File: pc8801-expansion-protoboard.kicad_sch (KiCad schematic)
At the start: 35 parts, among them J1 Solder Side, J2 Parts Side, J3 5V, J4 12V, J5 -12V, J6 GND_1, J7 GND_2, U1 ExpansionEdge, U10 74LS165, U11 ESP32-DEVKITC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

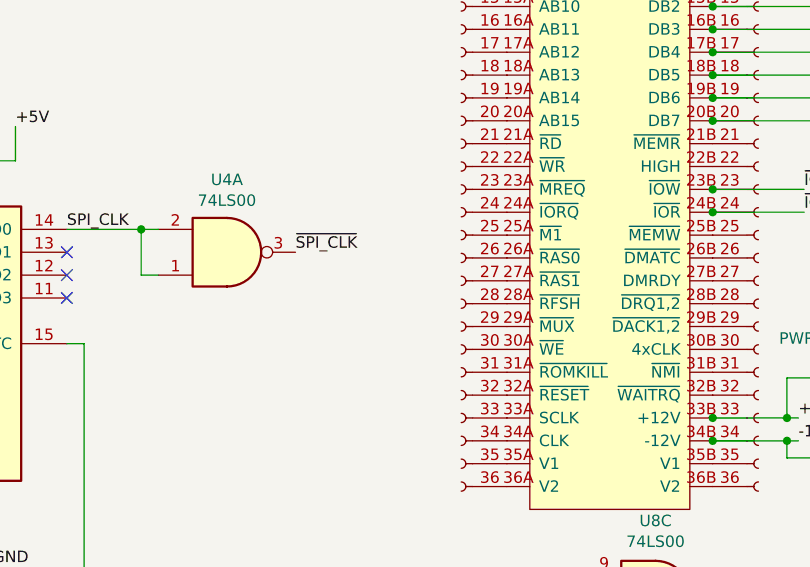
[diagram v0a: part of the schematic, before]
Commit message: Fix swapped-side near disaster
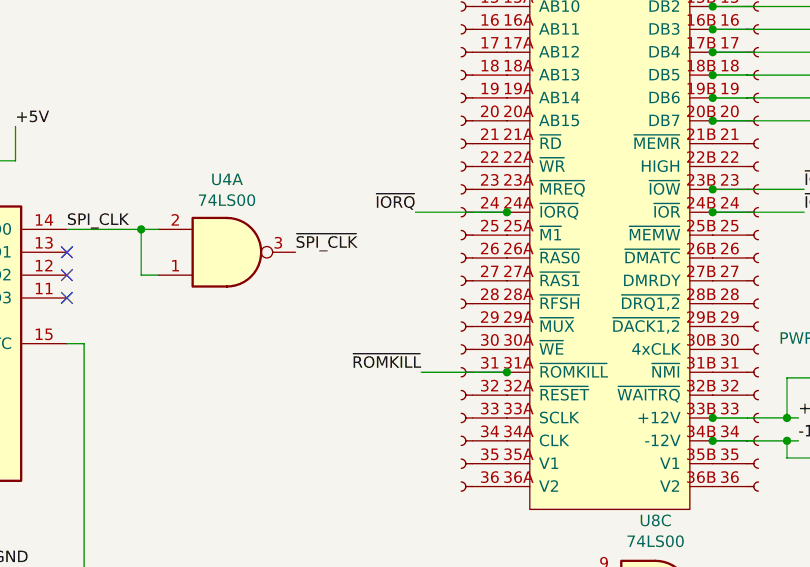
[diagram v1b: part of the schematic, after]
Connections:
- net ~{IORQ}: now reaches J1.24 (Pin_24), U1.24A (~{IORQ})
- net ~{ROMKILL}: now reaches J1.31 (Pin_31), U1.31A (~{ROMKILL})
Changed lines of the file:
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@@
   (junction (at 158.75 131.445) (diameter 0) (color 0 0 0 0)
   )
+  (junction (at 135.89 106.045) (diameter 0) (color 0 0 0 0)
+  )
   (junction (at 135.89 52.705) (diameter 0) (color 0 0 0 0)
   )
@@
   )
   (junction (at 135.89 60.325) (diameter 0) (color 0 0 0 0)
+  )
+  (junction (at 135.89 123.825) (diameter 0) (color 0 0 0 0)
   )
   (junction (at 231.14 133.35) (diameter 0) (color 0 0 0 0)
@@
     (stroke (width 0) (type default) (color 0 0 0 0))
   )
+  (wire (pts (xy 126.365 123.825) (xy 135.89 123.825))
+    (stroke (width 0) (type default) (color 0 0 0 0))
+  )
   (wire (pts (xy 81.28 96.52) (xy 81.28 100.33))
     (stroke (width 0) (type default) (color 0 0 0 0))
@@
   )
   (wire (pts (xy 55.88 163.195) (xy 55.88 160.02))
+    (stroke (width 0) (type default) (color 0 0 0 0))
+  )
+  (wire (pts (xy 125.73 106.045) (xy 135.89 106.045))
     (stroke (width 0) (type default) (color 0 0 0 0))
   )
@@
     (effects (font (size 1.27 1.27)) (justify right bottom))
   )
+  (label "~{IORQ}" (at 125.73 106.045 180)
+    (effects (font (size 1.27 1.27)) (justify right bottom))
+  )
   (label "D2" (at 179.705 83.185 0)
     (effects (font (size 1.27 1.27)) (justify left bottom))
@@
     (effects (font (size 1.27 1.27)) (justify left bottom))
   )
+  (label "~{ROMKILL}" (at 126.365 123.825 180)
+    (effects (font (size 1.27 1.27)) (justify right bottom))
+  )
   (label "GND" (at 140.335 240.03 0)

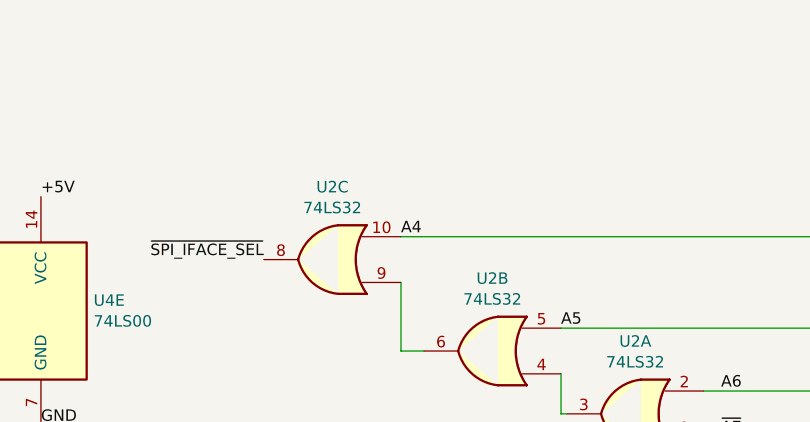
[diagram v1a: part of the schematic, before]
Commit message: Rewire and add test points
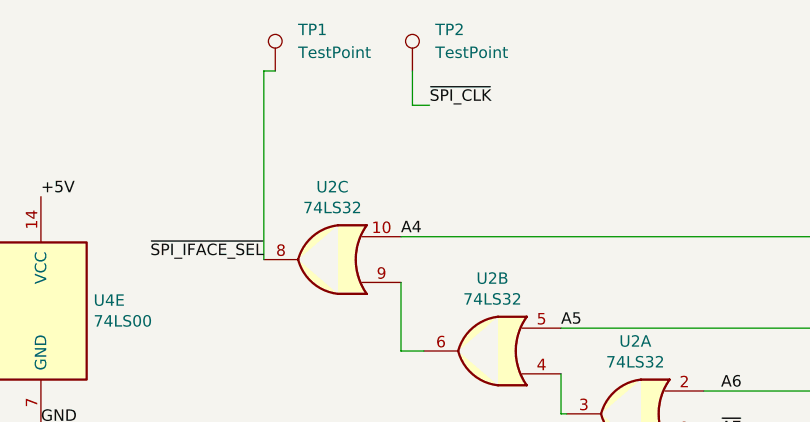
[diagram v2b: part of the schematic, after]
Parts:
- added TP1, TP2: TestPoint, TestPoint:TestPoint_Loop_D2.60mm_Drill1.4mm_Beaded, symbol Connector:TestPoint
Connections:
- net ~{SPI_CLK}: now also TP2.1
- net ~{SPI_IFACE_SEL}: now also TP1.1
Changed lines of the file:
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@@
+    (stroke (width 0) (type default) (color 0 0 0 0))
+  )
+  (wire (pts (xy 46.99 48.26) (xy 46.99 27.305))
     (stroke (width 0) (type default) (color 0 0 0 0))
   )
@@
     (stroke (width 0) (type default) (color 0 0 0 0))
   )
+  (wire (pts (xy 63.5 31.115) (xy 63.5 27.305))
+    (stroke (width 0) (type default) (color 0 0 0 0))
+  )
   (wire (pts (xy 158.75 88.265) (xy 188.595 88.265))
     (stroke (width 0) (type default) (color 0 0 0 0))
@@
     (stroke (width 0) (type default) (color 0 0 0 0))
   )
+  (wire (pts (xy 65.405 31.115) (xy 63.5 31.115))
+    (stroke (width 0) (type default) (color 0 0 0 0))
+  )
   (wire (pts (xy 158.75 55.245) (xy 178.435 55.245))
     (stroke (width 0) (type default) (color 0 0 0 0))
@@
   )
   (wire (pts (xy 165.735 189.865) (xy 170.18 189.865))
+    (stroke (width 0) (type default) (color 0 0 0 0))
+  )
+  (wire (pts (xy 46.99 27.305) (xy 48.26 27.305))
     (stroke (width 0) (type default) (color 0 0 0 0))
   )
@@
   )
   (label "-12V" (at 168.275 131.445 0)
+    (effects (font (size 1.27 1.27)) (justify left bottom))
+  )
+  (label "~{SPI_CLK}" (at 65.405 31.115 0)
     (effects (font (size 1.27 1.27)) (justify left bottom))
   )
@@
     (pin "1")
   )
+  (symbol (lib_id "Connector:TestPoint") (at 63.5 27.305 0) (unit 1)
+    (in_bom yes) (on_board yes) (fields_autoplaced)
+    (property "Reference" "TP2" (id 0) (at 66.04 22.7329 0)
+      (effects (font (size 1.27 1.27)) (justify left))
+    )
+    (property "Value" "TestPoint" (id 1) (at 66.04 25.2729 0)
+      (effects (font (size 1.27 1.27)) (justify left))
+    )
+    (property "Footprint" "TestPoint:TestPoint_Loop_D2.60mm_Drill1.4mm_Beaded" (id 2) (at 68.58 27.305 0)
+      (effects (font (size 1.27 1.27)) hide)
+    )
+    (property "Datasheet" "~" (id 3) (at 68.58 27.305 0)
+      (effects (font (size 1.27 1.27)) hide)
+    )
+    (pin "1")
+  )
   (symbol (lib_id "Device:LED") (at 147.32 257.81 180) (unit 1)
     (in_bom yes) (on_board yes) (fields_autoplaced)
@@
     (pin "2")
   )
+  (symbol (lib_id "Connector:TestPoint") (at 48.26 27.305 0) (unit 1)
+    (in_bom yes) (on_board yes) (fields_autoplaced)
+    (property "Reference" "TP1" (id 0) (at 50.8 22.7329 0)
+      (effects (font (size 1.27 1.27)) (justify left))
+    )
+    (property "Value" "TestPoint" (id 1) (at 50.8 25.2729 0)
+      (effects (font (size 1.27 1.27)) (justify left))
+    )
+    (property "Footprint" "TestPoint:TestPoint_Loop_D2.60mm_Drill1.4mm_Beaded" (id 2) (at 53.34 27.305 0)
+      (effects (font (size 1.27 1.27)) hide)
+    )
+    (property "Datasheet" "~" (id 3) (at 53.34 27.305 0)
+      (effects (font (size 1.27 1.27)) hide)
+    )
+    (pin "1")
+  )
   (symbol (lib_id "Device:R_Small_US") (at 138.43 257.81 90) (unit 1)
     (in_bom yes) (on_board yes) (fields_autoplaced)
@@
       (reference "R2") (unit 1) (value "560Ω") (footprint "Resistor_THT:R_Axial_DIN0207_L6.3mm_D2.5mm_P10.16mm_Horizontal")
     )
+    (path "/e10a8197-feb1-49a8-8ce1-531c3527f182"
+      (reference "TP1") (unit 1) (value "TestPoint") (footprint "TestPoint:TestPoint_Loop_D2.60mm_Drill1.4mm_Beaded")
+    )
+    (path "/39f8f47b-1e26-4975-b4fd-b1002648ab5b"
+      (reference "TP2") (unit 1) (value "TestPoint") (footprint "TestPoint:TestPoint_Loop_D2.60mm_Drill1.4mm_Beaded")
+    )
     (path "/00000000-0000-0000-0000-000061c04125"

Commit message: V0.2 for FujiNet sent to JLCPCB
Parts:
- added D2: LED, LED_THT:LED_D3.0mm, symbol Device:LED
- added R3: 560Ω, Resistor_THT:R_Axial_DIN0207_L6.3mm_D2.5mm_P10.16mm_Horizontal, symbol Device:R_Small_US
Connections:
- net GND: now also D2.1 (K)
- net at U11.24 (IO2): now also R3.1
- new net: D2.2 (A), R3.2
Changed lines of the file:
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@@
   (junction (at 158.75 80.645) (diameter 0) (color 0 0 0 0)
+  )
+  (junction (at 155.575 260.35) (diameter 0) (color 0 0 0 0)
   )
   (junction (at 178.435 47.625) (diameter 0) (color 0 0 0 0)
@@
     (stroke (width 0) (type default) (color 0 0 0 0))
   )
+  (wire (pts (xy 135.89 262.255) (xy 135.89 260.35))
+    (stroke (width 0) (type default) (color 0 0 0 0))
+  )
   (wire (pts (xy 168.91 106.045) (xy 158.75 106.045))
     (stroke (width 0) (type default) (color 0 0 0 0))
@@
     (stroke (width 0) (type default) (color 0 0 0 0))
   )
+  (wire (pts (xy 135.89 260.35) (xy 133.35 260.35))
+    (stroke (width 0) (type default) (color 0 0 0 0))
+  )
   (wire (pts (xy 215.9 90.805) (xy 208.915 90.805))
     (stroke (width 0) (type default) (color 0 0 0 0))
@@
     (stroke (width 0) (type default) (color 0 0 0 0))
   )
+  (wire (pts (xy 140.97 262.255) (xy 143.51 262.255))
+    (stroke (width 0) (type default) (color 0 0 0 0))
+  )
   (wire (pts (xy 122.555 65.405) (xy 135.89 65.405))
     (stroke (width 0) (type default) (color 0 0 0 0))
@@
     (stroke (width 0) (type default) (color 0 0 0 0))
   )
+  (wire (pts (xy 153.67 262.255) (xy 153.67 260.35))
+    (stroke (width 0) (type default) (color 0 0 0 0))
+  )
   (wire (pts (xy 26.67 160.655) (xy 26.67 163.195))
     (stroke (width 0) (type default) (color 0 0 0 0))
@@
     (stroke (width 0) (type default) (color 0 0 0 0))
   )
+  (wire (pts (xy 151.13 262.255) (xy 153.67 262.255))
+    (stroke (width 0) (type default) (color 0 0 0 0))
+  )
   (wire (pts (xy 57.785 125.73) (xy 57.785 123.19))
     (stroke (width 0) (type default) (color 0 0 0 0))
@@
     (stroke (width 0) (type default) (color 0 0 0 0))
   )
-  (wire (pts (xy 155.575 257.81) (xy 155.575 262.255))
+  (wire (pts (xy 155.575 257.81) (xy 155.575 260.35))
     (stroke (width 0) (type default) (color 0 0 0 0))
   )
@@
     (stroke (width 0) (type default) (color 0 0 0 0))
   )
+  (wire (pts (xy 155.575 260.35) (xy 155.575 262.255))
+    (stroke (width 0) (type default) (color 0 0 0 0))
+  )
   (wire (pts (xy 144.78 186.055) (xy 140.97 186.055))
     (stroke (width 0) (type default) (color 0 0 0 0))
@@
   )
   (wire (pts (xy 167.005 131.445) (xy 168.275 131.445))
+    (stroke (width 0) (type default) (color 0 0 0 0))
+  )
+  (wire (pts (xy 153.67 260.35) (xy 155.575 260.35))
     (stroke (width 0) (type default) (color 0 0 0 0))
   )
@@
     (pin "1")
   )
+  (symbol (lib_id "Device:LED") (at 147.32 262.255 180) (unit 1)
+    (in_bom yes) (on_board yes)
+    (property "Reference" "D2" (id 0) (at 147.32 267.335 0))
+    (property "Value" "LED" (id 1) (at 147.32 264.795 0))
+    (property "Footprint" "LED_THT:LED_D3.0mm" (id 2) (at 147.32 262.255 0)
+      (effects (font (size 1.27 1.27)) hide)
+    )
+    (property "Datasheet" "~" (id 3) (at 147.32 262.255 0)
+      (effects (font (size 1.27 1.27)) hide)
+    )
+    (pin "1")
+    (pin "2")
+  )
   (symbol (lib_id "Device:LED") (at 147.32 257.81 180) (unit 1)
     (in_bom yes) (on_board yes) (fields_autoplaced)
@@
     (pin "2")
   )
+  (symbol (lib_id "Device:R_Small_US") (at 138.43 262.255 90) (unit 1)
+    (in_bom yes) (on_board yes)
+    (property "Reference" "R3" (id 0) (at 138.43 266.7 90))
+    (property "Value" "560Ω" (id 1) (at 138.43 264.795 90))
+    (property "Footprint" "Resistor_THT:R_Axial_DIN0207_L6.3mm_D2.5mm_P10.16mm_Horizontal" (id 2) (at 138.43 262.255 0)
+      (effects (font (size 1.27 1.27)) hide)
+    )
+    (property "Datasheet" "~" (id 3) (at 138.43 262.255 0)
+      (effects (font (size 1.27 1.27)) hide)
+    )
+    (pin "1")
+    (pin "2")
+  )
   (sheet_instances
     (path "/" (page "1"))
@@
       (reference "D1") (unit 1) (value "LED") (footprint "LED_THT:LED_D3.0mm")
     )
+    (path "/6e8e4a3a-50f7-4e70-bb89-573181069e8d"
+      (reference "D2") (unit 1) (value "LED") (footprint "LED_THT:LED_D3.0mm")
+    )
     (path "/00000000-0000-0000-0000-000061c06ab2"
       (reference "J1") (unit 1) (value "Solder Side") (footprint "Connector_PinHeader_2.54mm:PinHeader_1x36_P2.54mm_Vertical")
@@
       (reference "R2") (unit 1) (value "560Ω") (footprint "Resistor_THT:R_Axial_DIN0207_L6.3mm_D2.5mm_P10.16mm_Horizontal")
     )
+    (path "/f5085a91-2c3d-4f5c-900f-9ea6af63a392"
+      (reference "R3") (unit 1) (value "560Ω") (footprint "Resistor_THT:R_Axial_DIN0207_L6.3mm_D2.5mm_P10.16mm_Horizontal")
+    )
     (path "/e10a8197-feb1-49a8-8ce1-531c3527f182"

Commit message: Fix too-tiny R1
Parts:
- R1: footprint Resistor_THT:R_Axial_DIN0204_L3.6mm_D1.6mm_P7.62mm_Horizontal -> Resistor_THT:R_Axial_DIN0207_L6.3mm_D2.5mm_P10.16mm_Horizontal
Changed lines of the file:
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@@
     (property "Reference" "R1" (id 0) (at 167.64 181.483 90))
     (property "Value" "10kΩ" (id 1) (at 167.64 183.7944 90))
-    (property "Footprint" "Resistor_THT:R_Axial_DIN0204_L3.6mm_D1.6mm_P7.62mm_Horizontal" (id 2) (at 167.64 186.69 0)
+    (property "Footprint" "Resistor_THT:R_Axial_DIN0207_L6.3mm_D2.5mm_P10.16mm_Horizontal" (id 2) (at 167.64 186.69 0)
       (effects (font (size 1.27 1.27)) hide)
     )
@@
     )
     (path "/00000000-0000-0000-0000-000062ccaf1b"
-      (reference "R1") (unit 1) (value "10kΩ") (footprint "Resistor_THT:R_Axial_DIN0204_L3.6mm_D1.6mm_P7.62mm_Horizontal")
+      (reference "R1") (unit 1) (value "10kΩ") (footprint "Resistor_THT:R_Axial_DIN0207_L6.3mm_D2.5mm_P10.16mm_Horizontal")
     )
     (path "/e40129d7-8674-459d-9e84-03538bf9687e"

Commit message: reset button
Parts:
- added SW1: Reset ESP, Button_Switch_THT:SW_PUSH_6mm, symbol Switch:SW_Push
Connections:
- net GND: now also SW1.1
- net ~{ESP_RESET}: now reaches U11.2 (EN)
- net ~{ESP_RESET}: now also SW1.2
- no-connect marks 15 -> 38
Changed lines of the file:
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@@
   (junction (at 135.89 50.165) (diameter 0) (color 0 0 0 0)
   )
-  (no_connect (at 92.71 227.33))
   (no_connect (at 92.71 224.79))
   (no_connect (at 92.71 232.41))
@@
   (no_connect (at 263.525 80.01))
   (no_connect (at 86.995 110.49))
+  (no_connect (at 92.71 234.95))
+  (no_connect (at 92.71 237.49))
+  (no_connect (at 92.71 240.03))
+  (no_connect (at 92.71 242.57))
+  (no_connect (at 133.35 250.19))
+  (no_connect (at 133.35 252.73))
+  (no_connect (at 133.35 255.27))
+  (no_connect (at 133.35 262.89))
+  (no_connect (at 133.35 270.51))
+  (no_connect (at 133.35 267.97))
+  (no_connect (at 133.35 265.43))
+  (no_connect (at 133.35 229.87))
+  (no_connect (at 133.35 232.41))
+  (no_connect (at 133.35 234.95))
+  (no_connect (at 133.35 237.49))
+  (no_connect (at 92.71 267.97))
+  (no_connect (at 92.71 265.43))
+  (no_connect (at 92.71 262.89))
+  (no_connect (at 92.71 260.35))
+  (no_connect (at 92.71 245.11))
+  (no_connect (at 92.71 247.65))
+  (no_connect (at 92.71 250.19))
+  (no_connect (at 92.71 252.73))
+  (no_connect (at 92.71 255.27))
   (no_connect (at 40.005 82.55))
   (no_connect (at 188.595 100.965))
@@
     (stroke (width 0) (type default) (color 0 0 0 0))
   )
+  (wire (pts (xy 84.455 227.33) (xy 84.455 220.98))
+    (stroke (width 0) (type default) (color 0 0 0 0))
+  )
   (wire (pts (xy 135.89 70.485) (xy 111.76 70.485))
     (stroke (width 0) (type default) (color 0 0 0 0))
@@
     (stroke (width 0) (type default) (color 0 0 0 0))
   )
+  (wire (pts (xy 64.77 220.98) (xy 67.31 220.98))
+    (stroke (width 0) (type default) (color 0 0 0 0))
+  )
   (wire (pts (xy 163.83 186.69) (xy 163.83 184.15))
     (stroke (width 0) (type default) (color 0 0 0 0))
@@
     (stroke (width 0) (type default) (color 0 0 0 0))
   )
+  (wire (pts (xy 64.77 231.14) (xy 64.77 220.98))
+    (stroke (width 0) (type default) (color 0 0 0 0))
+  )
   (wire (pts (xy 305.435 92.075) (xy 309.245 92.075))
     (stroke (width 0) (type default) (color 0 0 0 0))
@@
     (stroke (width 0) (type default) (color 0 0 0 0))
   )
+  (wire (pts (xy 92.71 227.33) (xy 84.455 227.33))
+    (stroke (width 0) (type default) (color 0 0 0 0))
+  )
   (wire (pts (xy 26.67 152.4) (xy 33.655 152.4))
     (stroke (width 0) (type default) (color 0 0 0 0))
@@
   )
   (wire (pts (xy 158.75 85.725) (xy 188.595 85.725))
+    (stroke (width 0) (type default) (color 0 0 0 0))
+  )
+  (wire (pts (xy 84.455 220.98) (xy 77.47 220.98))
     (stroke (width 0) (type default) (color 0 0 0 0))
   )
@@
   )
   (label "~{START}" (at 129.54 157.48 0)
+    (effects (font (size 1.27 1.27)) (justify left bottom))
+  )
+  (label "~{ESP_RESET}" (at 80.01 220.98 0)
     (effects (font (size 1.27 1.27)) (justify left bottom))
   )
@@
     (pin "1")
   )
+  (symbol (lib_id "power:GND") (at 64.77 231.14 0) (unit 1)
+    (in_bom yes) (on_board yes) (fields_autoplaced)
+    (property "Reference" "#PWR0101" (id 0) (at 64.77 237.49 0)
+      (effects (font (size 1.27 1.27)) hide)
+    )
+    (property "Value" "GND" (id 1) (at 64.77 236.22 0))
+    (property "Footprint" "" (id 2) (at 64.77 231.14 0)
+      (effects (font (size 1.27 1.27)) hide)
+    )
+    (property "Datasheet" "" (id 3) (at 64.77 231.14 0)
+      (effects (font (size 1.27 1.27)) hide)
+    )
+    (pin "1")
+  )
   (symbol (lib_id "Device:LED") (at 147.32 262.255 180) (unit 1)
     (in_bom yes) (on_board yes)
@@
     )
     (property "Datasheet" "~" (id 3) (at 147.32 262.255 0)
+      (effects (font (size 1.27 1.27)) hide)
+    )
+    (pin "1")
+    (pin "2")
+  )
+  (symbol (lib_id "Switch:SW_Push") (at 72.39 220.98 0) (unit 1)
+    (in_bom yes) (on_board yes) (fields_autoplaced)
+    (property "Reference" "SW1" (id 0) (at 72.39 213.36 0))
+    (property "Value" "Reset ESP" (id 1) (at 72.39 215.9 0))
+    (property "Footprint" "Button_Switch_THT:SW_PUSH_6mm" (id 2) (at 72.39 215.9 0)
+      (effects (font (size 1.27 1.27)) hide)
+    )
+    (property "Datasheet" "~" (id 3) (at 72.39 215.9 0)
       (effects (font (size 1.27 1.27)) hide)
     )
@@
       (reference "#FLG0104") (unit 1) (value "PWR_FLAG") (footprint "")
     )
+    (path "/5787e195-3b65-4af7-b0f0-aa4eb10c6c0f"
+      (reference "#PWR0101") (unit 1) (value "GND") (footprint "")
+    )
     (path "/00000000-0000-0000-0000-000062de6e49"
       (reference "C1") (unit 1) (value "10µF") (footprint "Capacitor_THT:CP_Radial_D5.0mm_P2.00mm")
@@
       (reference "R3") (unit 1) (value "560Ω") (footprint "Resistor_THT:R_Axial_DIN0207_L6.3mm_D2.5mm_P10.16mm_Horizontal")
     )
+    (path "/70f9fc47-c421-429e-8cdb-52e212c53c51"
+      (reference "SW1") (unit 1) (value "Reset ESP") (footprint "Button_Switch_THT:SW_PUSH_6mm")
+    )
     (path "/e10a8197-feb1-49a8-8ce1-531c3527f182"
